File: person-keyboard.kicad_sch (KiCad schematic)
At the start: 31 parts, among them J1 USB_C_Receptacle_USB2.0_16P, U1 RP2040, U2 AMS1117-3.3, U3 W25Q128JVS, U4 PRTR5V0U2X, Y1 ABM8-272-T3

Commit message: Starting work
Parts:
- added SW106, SW107: SW_Push, symbol Switch:SW_Push
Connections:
- net GND: now also SW106.1, SW107.1
- net at R7.1, U1.26 (RUN): now also SW106.2
- net at R3.1: now also SW107.2
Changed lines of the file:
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@@
+	)
+	(symbol
+		(lib_id "Switch:SW_Push")
+		(at 99.06 64.77 0)
+		(unit 1)
+		(exclude_from_sim no)
+		(in_bom yes)
+		(on_board yes)
+		(dnp no)
+		(fields_autoplaced yes)
+		(property "Reference" "SW106"
+			(at 99.06 57.15 0)
+			(effects
+				(font
+					(size 1.27 1.27)
+				)
+			)
+		)
+		(property "Value" "SW_Push"
+			(at 99.06 59.69 0)
+			(effects
+				(font
+					(size 1.27 1.27)
+				)
+			)
+		)
+		(property "Footprint" ""
+			(at 99.06 59.69 0)
+			(effects
+				(font
+					(size 1.27 1.27)
+				)
+				(hide yes)
+			)
+		)
+		(property "Datasheet" "~"
+			(at 99.06 59.69 0)
+			(effects
+				(font
+					(size 1.27 1.27)
+				)
+				(hide yes)
+			)
+		)
+		(property "Description" "Push button switch, generic, two pins"
+			(at 99.06 64.77 0)
+			(effects
+				(font
+					(size 1.27 1.27)
+				)
+				(hide yes)
+			)
+		)
+		(pin "2"
+		)
+		(pin "1"
+		)
+		(instances
+			(project ""
+				(path "/0b898f65-1e2f-4a4e-92cd-8ce3f937fe7d"
+					(reference "SW106")
+					(unit 1)
+				)
+			)
+		)
 	)
 	(symbol
@@
 					(unit 1)
 				)
+			)
+		)
+	)
+	(symbol
+		(lib_id "Switch:SW_Push")
+		(at 210.82 96.52 90)
+		(unit 1)
+		(exclude_from_sim no)
+		(in_bom yes)
+		(on_board yes)
+		(dnp no)
+		(fields_autoplaced yes)
+		(property "Reference" "SW107"
+			(at 212.09 95.2499 90)
+			(effects
+				(font
+					(size 1.27 1.27)
+				)
+				(justify right)
+			)
+		)
+		(property "Value" "SW_Push"
+			(at 212.09 97.7899 90)
+			(effects
+				(font
+					(size 1.27 1.27)
+				)
+				(justify right)
+			)
+		)
+		(property "Footprint" ""
+			(at 205.74 96.52 0)
+			(effects
+				(font
+					(size 1.27 1.27)
+				)
+				(hide yes)
+			)
+		)
+		(property "Datasheet" "~"
+			(at 205.74 96.52 0)
+			(effects
+				(font
+					(size 1.27 1.27)
+				)
+				(hide yes)
+			)
+		)
+		(property "Description" "Push button switch, generic, two pins"
+			(at 210.82 96.52 0)
+			(effects
+				(font
+					(size 1.27 1.27)
+				)
+				(hide yes)
+			)
+		)
+		(pin "2"
+		)
+		(pin "1"
+		)
+		(instances
+			(project "person-keyboard"
+				(path "/0b898f65-1e2f-4a4e-92cd-8ce3f937fe7d"
+					(reference "SW107")
+					(unit 1)
+				)

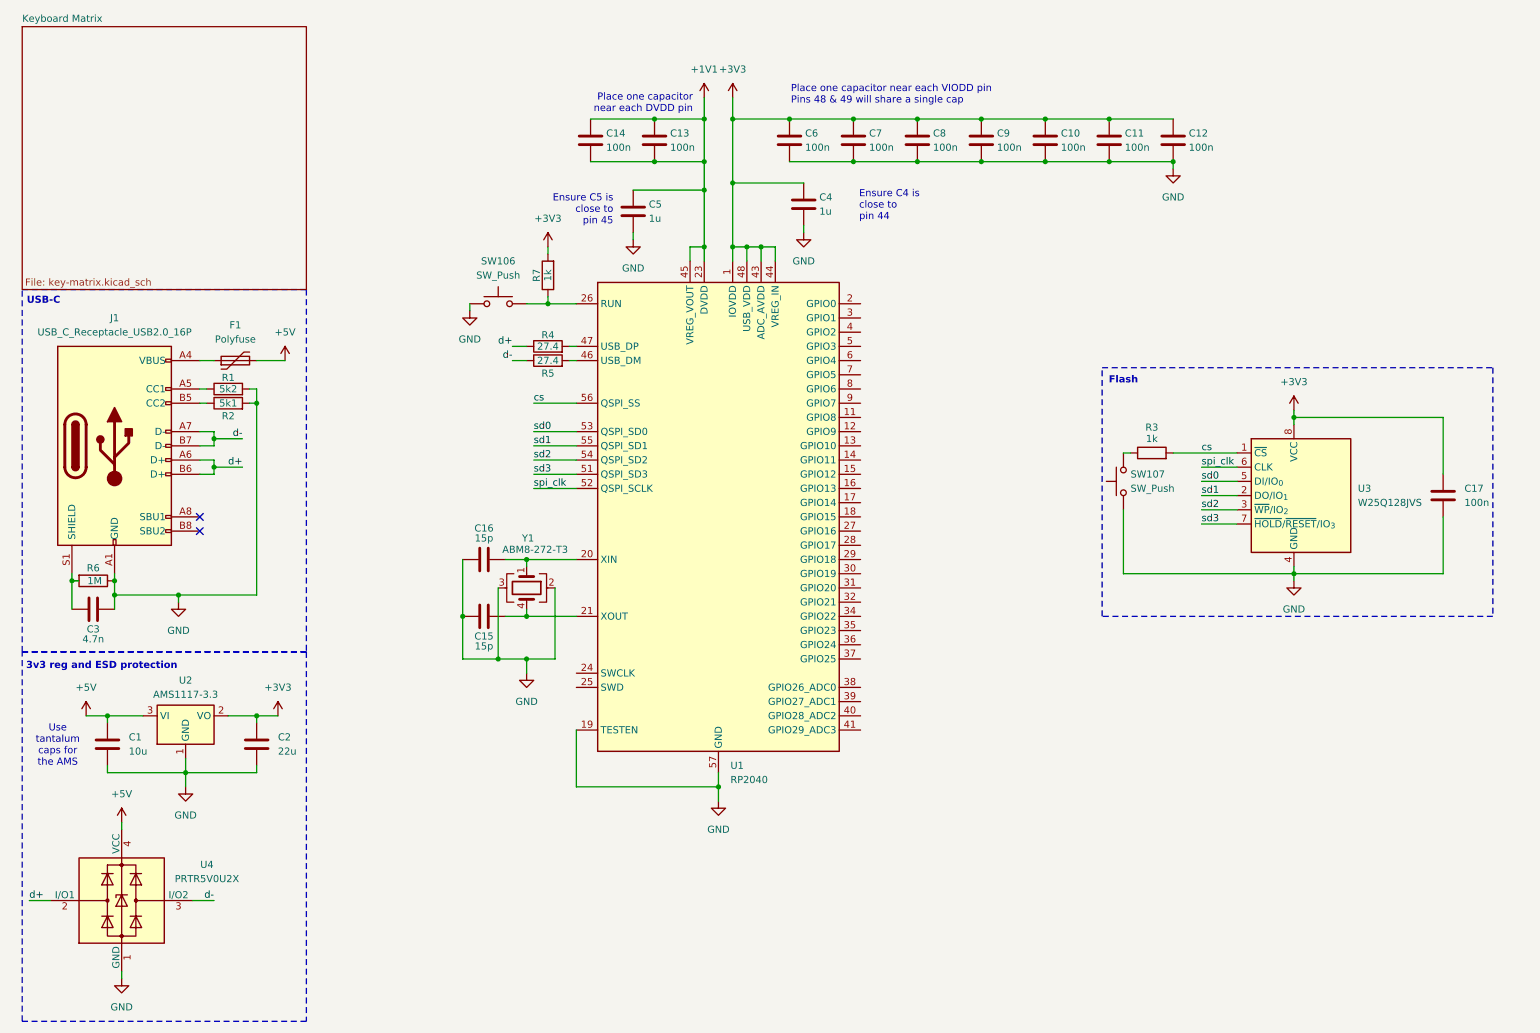
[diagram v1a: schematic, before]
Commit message: Fixed key matrix, laid out LED matrix, started laying out microcontroller
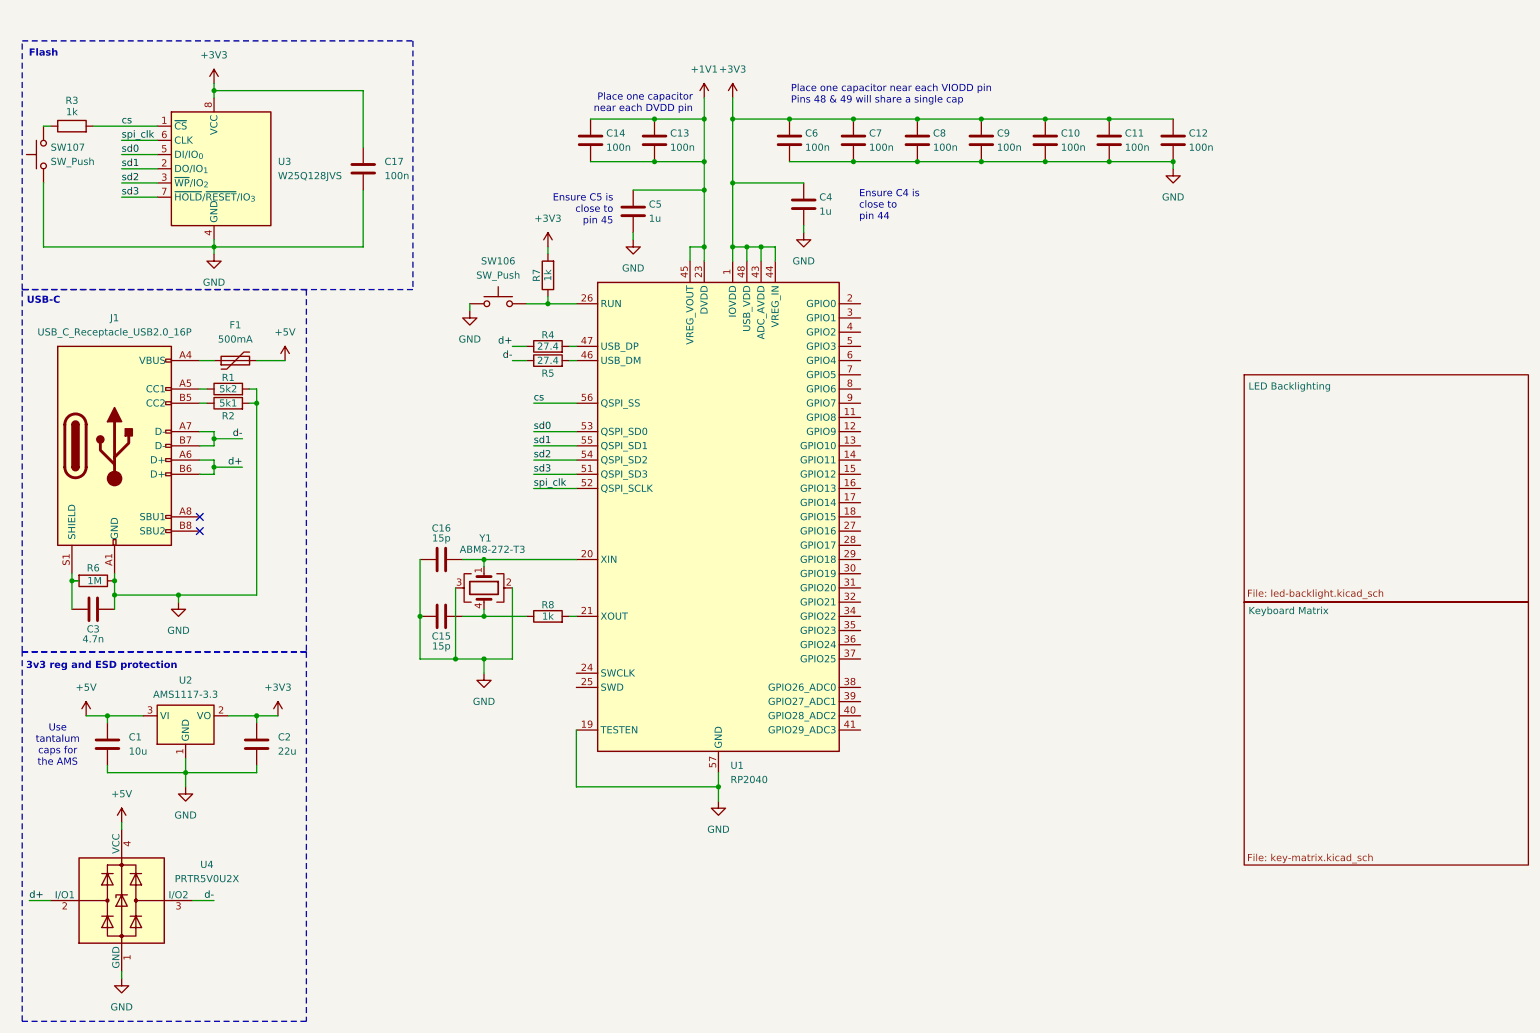
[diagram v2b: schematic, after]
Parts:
- added R8: 1k, Resistor_SMD:R_0402_1005Metric, symbol Device:R
- C1, C2: footprint (none) -> Capacitor_SMD:C_0805_2012Metric
- F1: value Polyfuse -> 500mA; footprint (none) -> Fuse:Fuse_0805_2012Metric
- J1: footprint (none) -> Connector_USB:USB_C_Receptacle_GCT_USB4105-xx-A_16P_TopMnt_Horizontal
- R1, R2, R6: footprint (none) -> Resistor_SMD:R_0805_2012Metric
- SW107: footprint (none) -> jacob-libs:SW-SMD_L4.0-W2.9-LS5.0
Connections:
- net at C15.2, Y1.4: now also R8.1; no longer U1.21 (XOUT)
- new net: R8.2, U1.21 (XOUT)
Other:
- added sheet LED Backlighting (led-backlight.kicad_sch)
- moved on the sheet: C15, C16, C17, R3, SW107, U3, Y1

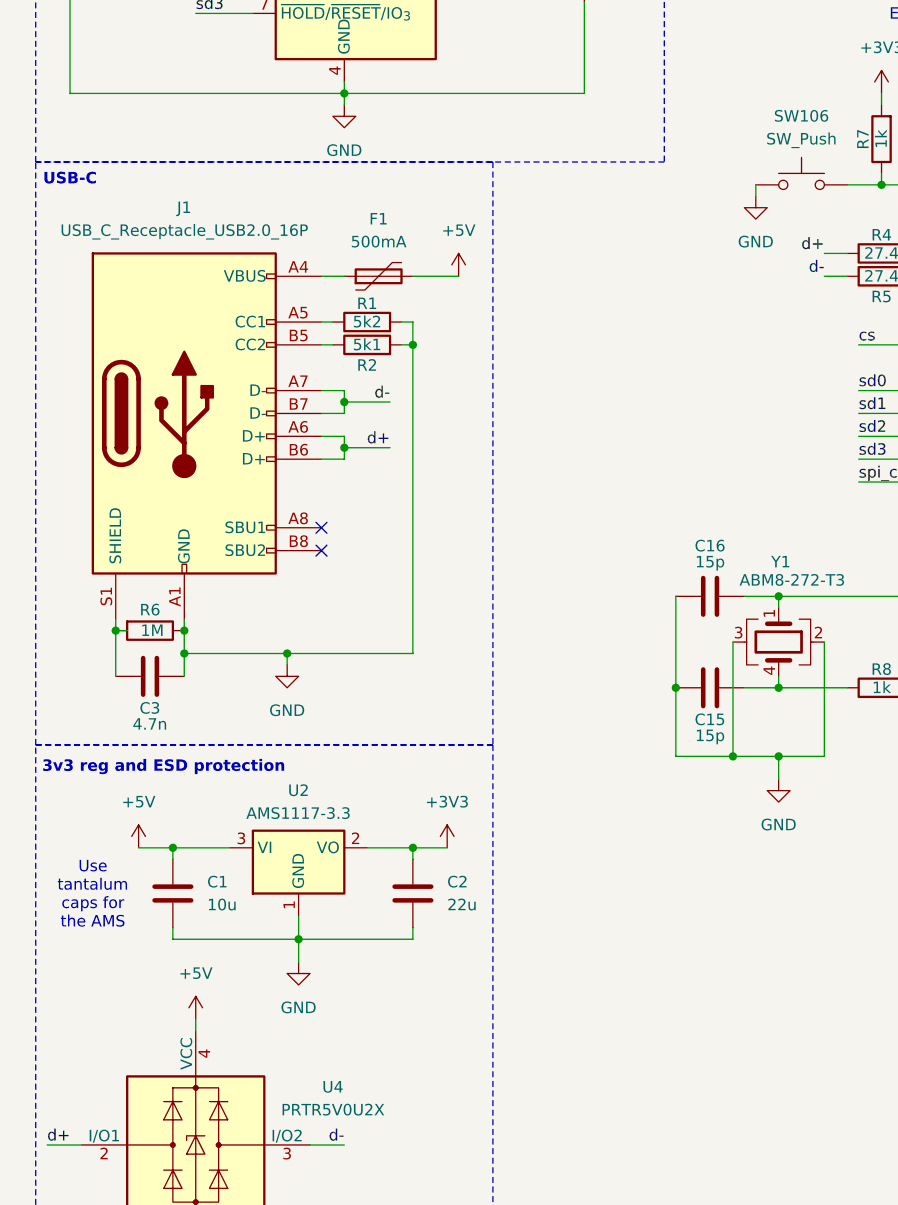
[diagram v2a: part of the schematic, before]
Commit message: Added protection diode, reconsidered mcu position
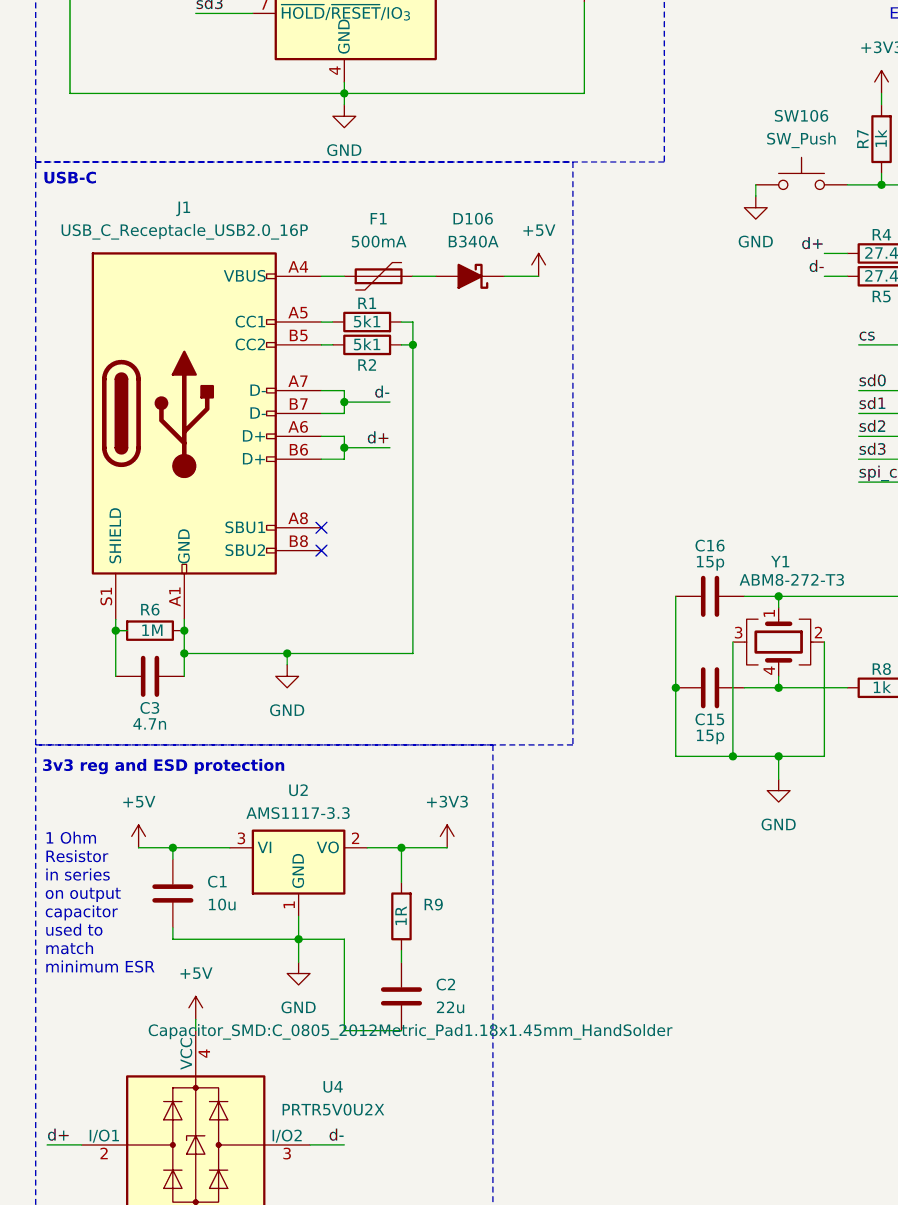
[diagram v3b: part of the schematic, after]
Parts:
- added D106: B340A, PCM_Diode_SMD_AKL:D_SMA, symbol PCM_Diode_Schottky_AKL:B340A
- added R9: 1R, Resistor_SMD:R_0805_2012Metric_Pad1.20x1.40mm_HandSolder, symbol Device:R
- C1, C2: footprint Capacitor_SMD:C_0805_2012Metric -> Capacitor_SMD:C_0805_2012Metric_Pad1.18x1.45mm_HandSolder
- C10, C11, C12, C13, C14, C15, C16, C17, C4, C5, C6, C7, C8, C9: footprint Capacitor_SMD:C_0402_1005Metric -> Capacitor_SMD:C_0402_1005Metric_Pad0.74x0.62mm_HandSolder
- R1: value 5k2 -> 5k1; footprint Resistor_SMD:R_0805_2012Metric -> Resistor_SMD:R_0805_2012Metric_Pad1.20x1.40mm_HandSolder
- R2: footprint Resistor_SMD:R_0805_2012Metric -> Resistor_SMD:R_0805_2012Metric_Pad1.20x1.40mm_HandSolder
- R8: footprint Resistor_SMD:R_0402_1005Metric -> Resistor_SMD:R_0402_1005Metric_Pad0.72x0.64mm_HandSolder
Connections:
- net +3V3: now also R9.2; no longer C2.1
- net +5V: now also D106.1 (K); no longer F1.2
- new net: C2.1, R9.1
- new net: D106.2 (A), F1.2
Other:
- note added: "1 Ohm Resistor in series on output capacitor used to match minimum ESR"
- note removed: "Use tantalum caps for the AMS"
- moved on the sheet: C2

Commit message: Routed microcontroller
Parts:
- removed D106: B340A, PCM_Diode_SMD_AKL:D_SMA, symbol PCM_Diode_Schottky_AKL:B340A
- added D106: 1N5819, Diode_SMD:D_SOD-123, symbol PCM_Diode_Schottky_AKL:D_Schottky_Generic
- C3: footprint (none) -> Capacitor_SMD:C_0805_2012Metric_Pad1.18x1.45mm_HandSolder
- SW106: footprint (none) -> jacob-libs:SW-SMD_L4.0-W2.9-LS5.0
- U1: footprint Package_DFN_QFN:QFN-56-1EP_7x7mm_P0.4mm_EP3.2x3.2mm -> jacob-libs:QFN-56-1EP_7x7mm_P0.4mm_EP3.2x3.2mm_vias
- Y1: symbol Device:Crystal_GND23 -> Device:Crystal_GND24
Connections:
- net +1V1: no longer C13.2, C14.2
- net +5V: now also D106.1 (K); no longer U4.4 (VCC)
- net GND: now also C13.2, C14.2, Y1.4; no longer Y1.3
- net at F1.2: now also D106.2 (A)
- net at C15.2, R8.1: now also Y1.3; no longer Y1.4
- net VCC: now reaches F1.1, J1.A4 (VBUS), J1.A9 (VBUS), J1.B4 (VBUS), J1.B9 (VBUS)
- net VCC: now also U4.4 (VCC)
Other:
- moved on the sheet: F1
